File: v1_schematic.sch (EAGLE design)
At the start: 124 parts, among them IC1 PCA82C250, IC2 FT232RL, IC3 SP3223EBP, IC4 MAX481CPA, IC5 LM2576T, Q1 25MHz, Q2 32.768kHz, Q3 2N2222A, T1 ST02-3.5MM, T3 2N2222, T4 2N2222, T5 2N2222, T6 2N2222, T7 2N2222, U1 ON_SEMICONDUCTOR_NCP1117ST33T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, U2 ON_SEMICONDUCTOR_NCP1117ST50T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, X1 MINI-USB-32005-201, X6 SDBMF, X7 5566-8, X8 5566-8

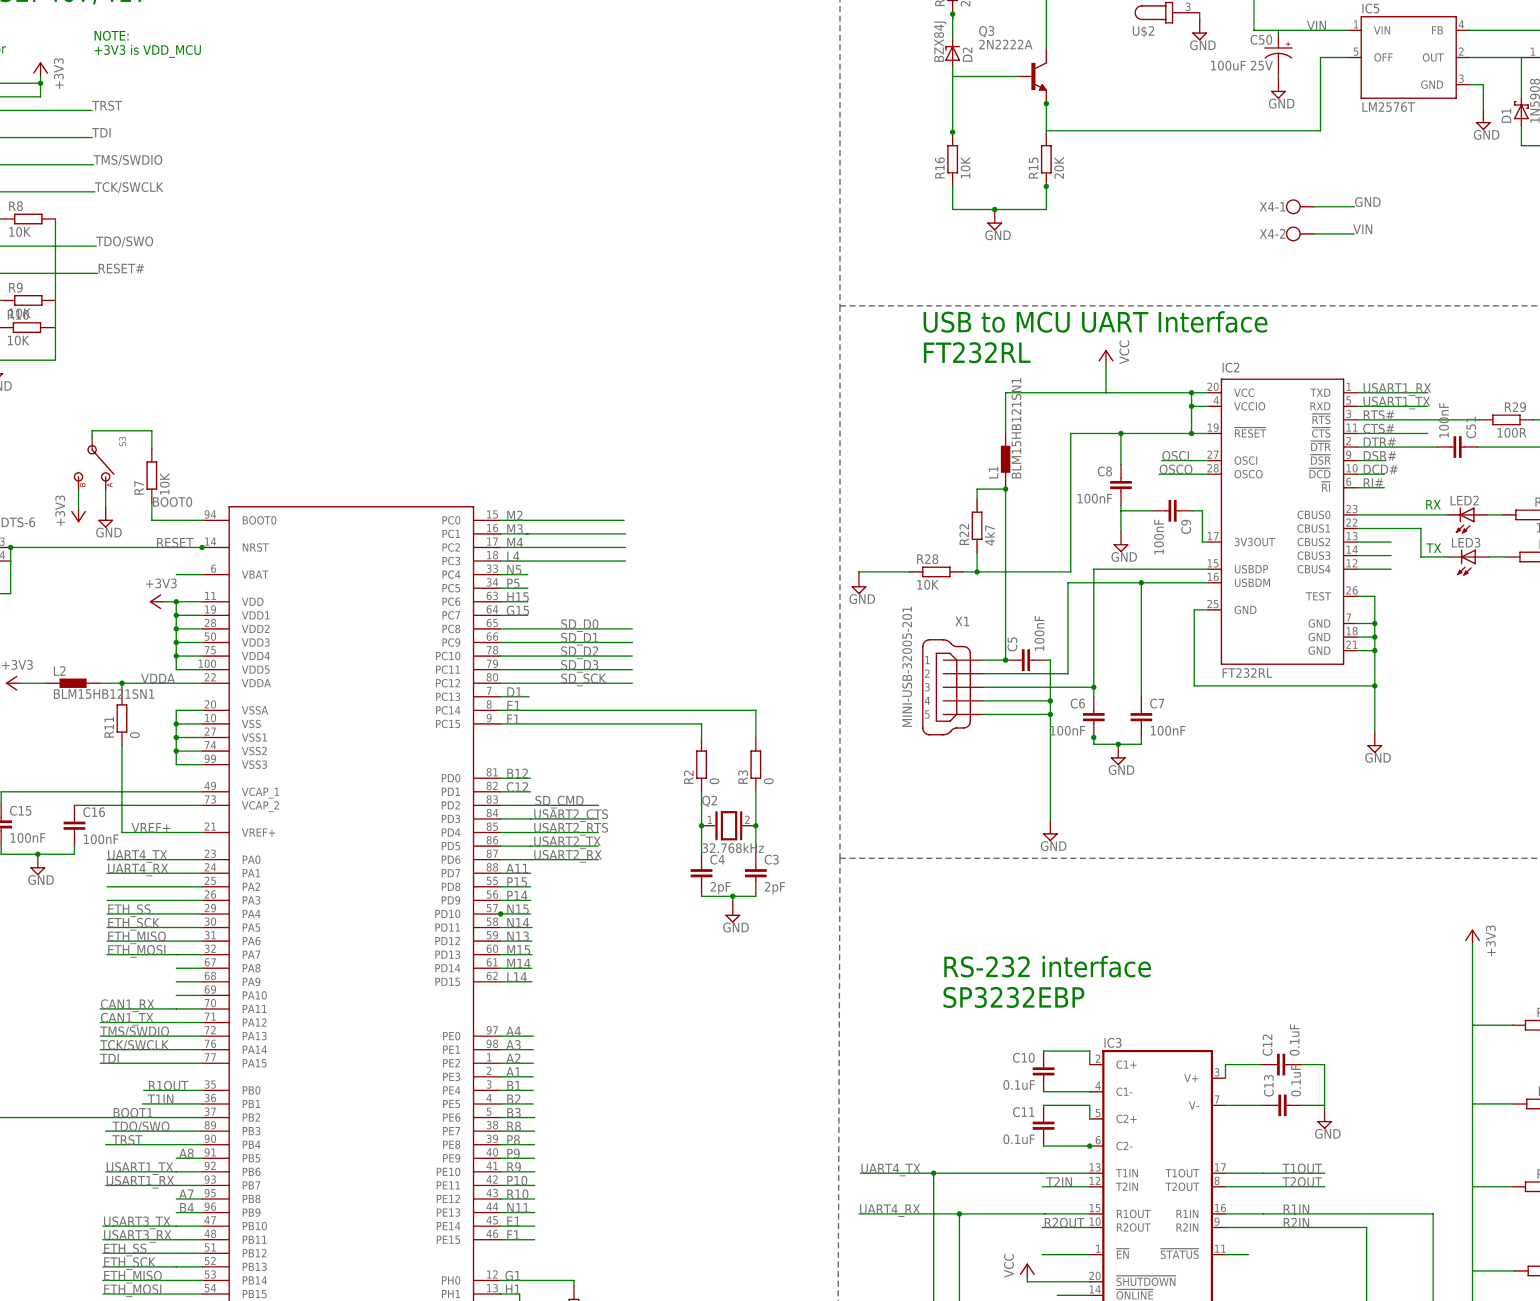
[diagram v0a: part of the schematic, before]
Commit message: NRF Interface and corrections
- Correction: Moved FT232 Interface to USART3
- Completed NRF interface to SPI1 of MCU (PB3-PB8)
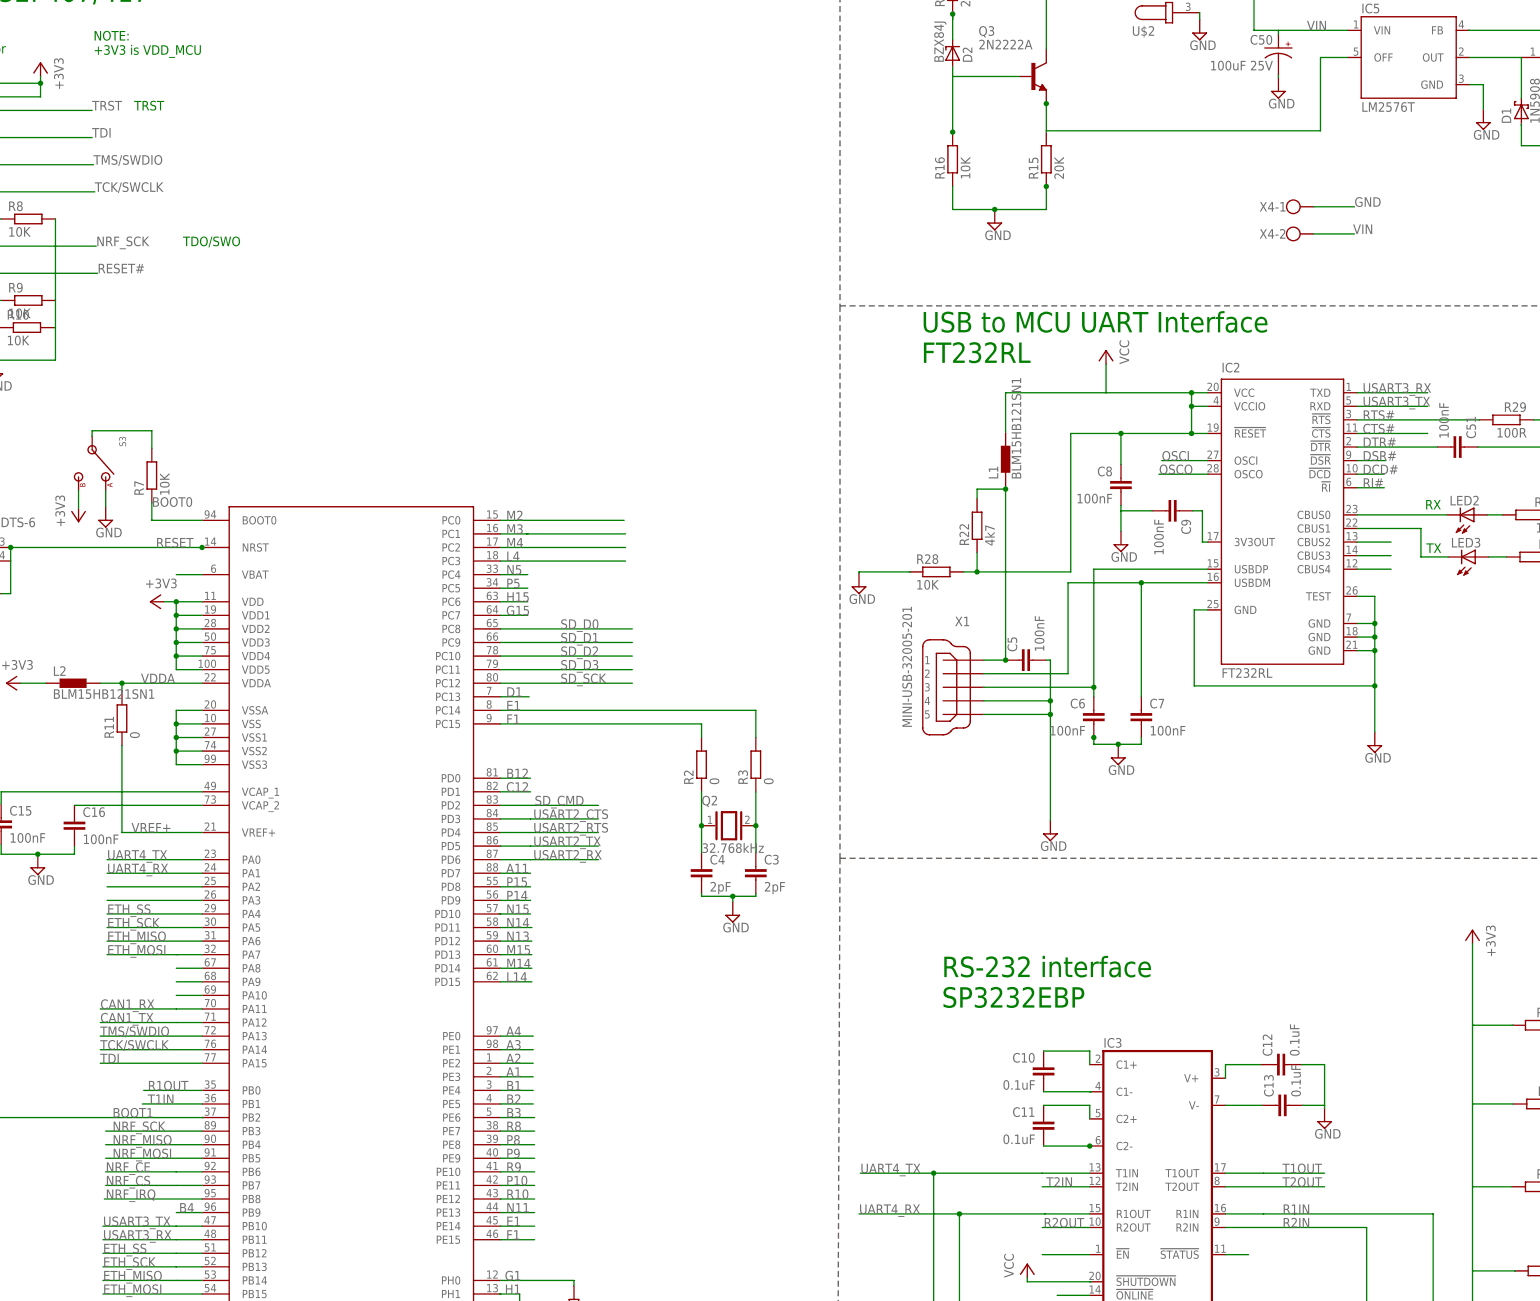
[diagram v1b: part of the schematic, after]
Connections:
- removed net A7: U$1.PB8
- removed net A8: U$1.PB5
- removed net TDO/SWO: J1.13, U$1.PB3
- removed net USART1_RX: IC2.TXD, U$1.PB7
- removed net USART1_TX: IC2.RXD, U$1.PB6
- net NRF_CE: now also U$1.PB6
- net NRF_CS: now also U$1.PB7
- net NRF_IRQ: now also U$1.PB8
- net NRF_MISO: now also U$1.PB4
- net NRF_MOSI: now also U$1.PB5
- net NRF_SCK: now also J1.13, U$1.PB3
- net TRST: no longer U$1.PB4
- net USART3_RX: now also IC2.TXD
- net USART3_TX: now also IC2.RXD
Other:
- note added: "TDO/SWO"
- note added: "TRST"
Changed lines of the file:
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@@
 <text x="154.432" y="31.75" size="3.81" layer="91">nRF5 Module Interface (nRF51822 Chip)</text>
 <text x="158.496" y="-25.654" size="3.81" layer="91">SD Card Interface</text>
+<text x="-221.996" y="156.464" size="1.778" layer="91" font="vector">TRST</text>
+<text x="-212.852" y="131.064" size="1.778" layer="91" font="vector">TDO/SWO</text>
 </plain>
 <instances>
@@
 </segment>
 </net>
-<net name="A8" class="0">
-<segment>
-<pinref part="U$1" gate="G$1" pin="PB5"/>
-<wire x1="-209.296" y1="-39.624" x2="-214.122" y2="-39.624" width="0.1524" layer="91"/>
-<label x="-213.614" y="-39.624" size="1.778" layer="95"/>
-</segment>
-</net>
-<net name="USART1_TX" class="0">
-<segment>
-<pinref part="U$1" gate="G$1" pin="PB6"/>
-<wire x1="-209.296" y1="-42.164" x2="-214.122" y2="-42.164" width="0.1524" layer="91"/>
-<label x="-227.33" y="-42.164" size="1.778" layer="95"/>
-<wire x1="-214.122" y1="-42.164" x2="-227.33" y2="-42.164" width="0.15" layer="91"/>
-</segment>
-<segment>
-<pinref part="IC2" gate="1" pin="RXD"/>
-<label x="7.874" y="101.092" size="1.778" layer="95"/>
-<wire x1="6.858" y1="101.092" x2="20.066" y2="101.092" width="0.1524" layer="91"/>
-</segment>
-</net>
-<net name="USART1_RX" class="0">
-<segment>
-<pinref part="U$1" gate="G$1" pin="PB7"/>
-<wire x1="-209.296" y1="-44.704" x2="-214.122" y2="-44.704" width="0.1524" layer="91"/>
-<label x="-227.33" y="-44.704" size="1.778" layer="95"/>
-<wire x1="-214.122" y1="-44.704" x2="-227.33" y2="-44.704" width="0.15" layer="91"/>
-</segment>
-<segment>
-<pinref part="IC2" gate="1" pin="TXD"/>
-<label x="7.874" y="103.632" size="1.778" layer="95"/>
-<wire x1="6.858" y1="103.632" x2="20.066" y2="103.632" width="0.1524" layer="91"/>
-</segment>
-</net>
-<net name="A7" class="0">
-<segment>
-<pinref part="U$1" gate="G$1" pin="PB8"/>
-<wire x1="-209.296" y1="-47.244" x2="-214.122" y2="-47.244" width="0.1524" layer="91"/>
-<label x="-213.614" y="-47.244" size="1.778" layer="95"/>
-</segment>
-</net>
 <net name="B4" class="0">
 <segment>
@@
 <wire x1="-214.122" y1="-52.324" x2="-227.838" y2="-52.324" width="0.15" layer="91"/>
 </segment>
+<segment>
+<pinref part="IC2" gate="1" pin="RXD"/>
+<label x="7.874" y="101.092" size="1.778" layer="95"/>
+<wire x1="6.858" y1="101.092" x2="20.066" y2="101.092" width="0.1524" layer="91"/>
+</segment>
 </net>
 <net name="USART3_RX" class="0">
@@
 <label x="-227.838" y="-54.864" size="1.778" layer="95"/>
 <wire x1="-214.122" y1="-54.864" x2="-227.838" y2="-54.864" width="0.15" layer="91"/>
+</segment>
+<segment>
+<pinref part="IC2" gate="1" pin="TXD"/>
+<label x="7.874" y="103.632" size="1.778" layer="95"/>
+<wire x1="6.858" y1="103.632" x2="20.066" y2="103.632" width="0.1524" layer="91"/>
 </segment>
 </net>
@@
 <pinref part="U$1" gate="G$1" pin="PD10"/>
 <wire x1="-153.416" y1="6.096" x2="-147.828" y2="6.096" width="0.1524" layer="91"/>
-<junction x="-153.416" y="6.096"/>
 </segment>
 </net>
@@
 <label x="-229.87" y="156.464" size="1.778" layer="95"/>
 </segment>
-<segment>
-<pinref part="U$1" gate="G$1" pin="PB4"/>
-<label x="-226.06" y="-37.084" size="1.778" layer="95"/>
-<wire x1="-209.296" y1="-37.084" x2="-227.33" y2="-37.084" width="0.1524" layer="91"/>
-</segment>
 </net>
 <net name="TDI" class="0">
@@
 <wire x1="-254.508" y1="136.144" x2="-246.888" y2="136.144" width="0.1524" layer="91"/>
 <pinref part="R8" gate="G$1" pin="1"/>
-</segment>
-</net>
-<net name="TDO/SWO" class="0">
-<segment>
-<pinref part="J1" gate="1" pin="13"/>
-<wire x1="-254.508" y1="131.064" x2="-229.108" y2="131.064" width="0.1524" layer="91"/>
-<label x="-229.108" y="131.064" size="1.778" layer="95"/>
-</segment>
-<segment>
-<pinref part="U$1" gate="G$1" pin="PB3"/>
-<label x="-226.06" y="-34.544" size="1.778" layer="95"/>
-<wire x1="-209.296" y1="-34.544" x2="-227.33" y2="-34.544" width="0.1524" layer="91"/>
 </segment>
 </net>
@@
 <junction x="203.708" y="13.208"/>
 </segment>
+<segment>
+<pinref part="U$1" gate="G$1" pin="PB6"/>
+<wire x1="-209.296" y1="-42.164" x2="-214.122" y2="-42.164" width="0.1524" layer="91"/>
+<label x="-227.33" y="-42.164" size="1.778" layer="95"/>
+<wire x1="-214.122" y1="-42.164" x2="-227.33" y2="-42.164" width="0.15" layer="91"/>
+</segment>
 </net>
 <net name="NRF_CS" class="0">
@@
 <junction x="203.708" y="10.668"/>
 </segment>
+<segment>
+<pinref part="U$1" gate="G$1" pin="PB7"/>
+<wire x1="-209.296" y1="-44.704" x2="-214.122" y2="-44.704" width="0.1524" layer="91"/>
+<label x="-227.33" y="-44.704" size="1.778" layer="95"/>
+<wire x1="-214.122" y1="-44.704" x2="-227.33" y2="-44.704" width="0.15" layer="91"/>
+</segment>
 </net>
 <net name="NRF_SCK" class="0">
@@
 <junction x="203.708" y="8.128"/>
 </segment>
+<segment>
+<pinref part="J1" gate="1" pin="13"/>
+<wire x1="-254.508" y1="131.064" x2="-229.108" y2="131.064" width="0.1524" layer="91"/>
+<label x="-229.108" y="131.064" size="1.778" layer="95"/>
+</segment>
+<segment>
+<pinref part="U$1" gate="G$1" pin="PB3"/>
+<label x="-226.06" y="-34.544" size="1.778" layer="95"/>
+<wire x1="-209.296" y1="-34.544" x2="-227.33" y2="-34.544" width="0.1524" layer="91"/>
+</segment>
 </net>
 <net name="NRF_MOSI" class="0">
@@
 <junction x="203.708" y="5.588"/>
 </segment>
+<segment>
+<pinref part="U$1" gate="G$1" pin="PB5"/>
+<label x="-226.06" y="-39.624" size="1.778" layer="95"/>
+<wire x1="-209.296" y1="-39.624" x2="-227.33" y2="-39.624" width="0.1524" layer="91"/>
+</segment>
 </net>
 <net name="NRF_MISO" class="0">
@@
 <junction x="203.708" y="3.048"/>
 </segment>
+<segment>
+<pinref part="U$1" gate="G$1" pin="PB4"/>
+<label x="-226.06" y="-37.084" size="1.778" layer="95"/>
+<wire x1="-209.296" y1="-37.084" x2="-227.33" y2="-37.084" width="0.1524" layer="91"/>
+</segment>
 </net>
 <net name="NRF_IRQ" class="0">
@@
 <junction x="203.708" y="0.508"/>
 </segment>
-</net>
+<segment>
+<pinref part="U$1" gate="G$1" pin="PB8"/>
+<label x="-227.33" y="-47.244" size="1.778" layer="95"/>
+<wire x1="-209.296" y1="-47.244" x2="-227.584" y2="-47.244" width="0.1524" layer="91"/>
+</segment>
+</net>
